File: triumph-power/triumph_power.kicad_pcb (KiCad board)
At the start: 2 copper layers, 43.2 x 30.5 mm, 13 parts, among them J1 JST_XH_vert_01x04, J2 JST_XH_vert_01x04

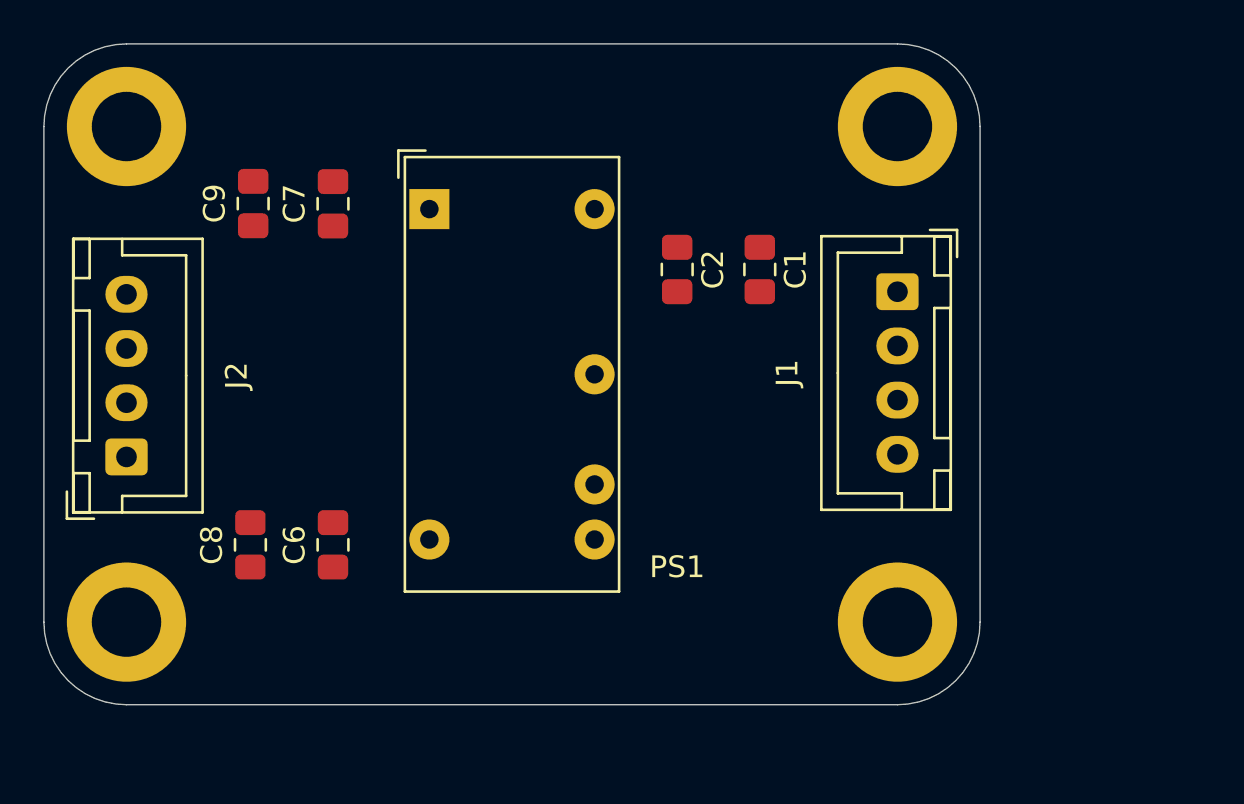
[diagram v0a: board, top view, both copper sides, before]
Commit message: Route power board
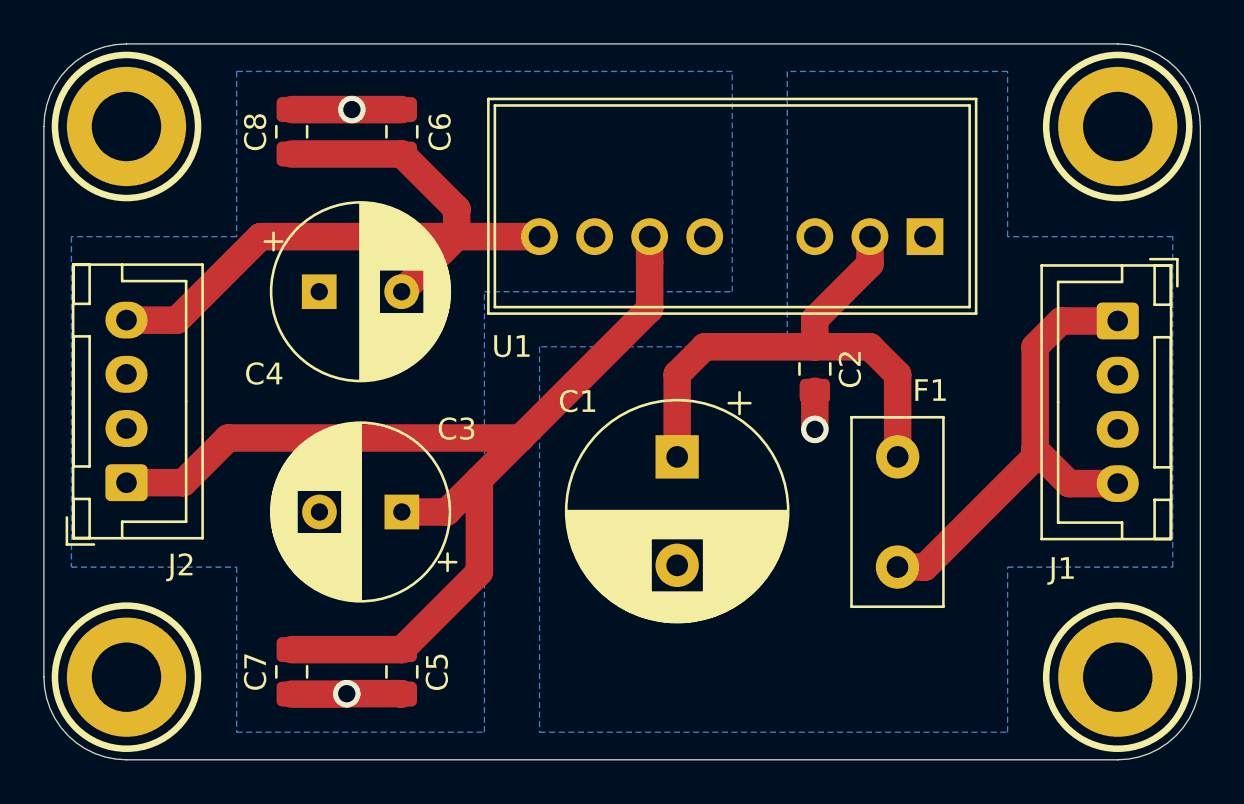
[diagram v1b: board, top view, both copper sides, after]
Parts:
- removed C9: 0.01uF, Capacitor_SMD:C_0805_2012Metric_Pad1.15x1.40mm_HandSolder
- removed PS1: RS-1212D, Converter_DCDC:Converter_DCDC_XP_POWER-IAxxxxD_THT
- added C3: 10uF, Capacitor_THT:CP_Radial_D8.0mm_P3.80mm, F.Cu at (139.7, 114.3)
- added C4: 10uF, Capacitor_THT:CP_Radial_D8.0mm_P3.80mm, F.Cu at (135.9, 104.1)
- added C5: 0.1uF, Capacitor_SMD:C_0805_2012Metric_Pad1.15x1.40mm_HandSolder, F.Cu at (139.7, 121.7)
- added F1: MF-R050, Fuse:Fuse_Littelfuse_395Series, F.Cu at (162.6, 116.8)
- added U1: RS-1212D, triumph:RS-xxxxD, F.Cu at (163.8, 101.6)
- C1: value 1uF -> 47uF; footprint Capacitor_SMD:C_0805_2012Metric_Pad1.15x1.40mm_HandSolder -> Capacitor_THT:CP_Radial_D10.0mm_P5.00mm
- C7: value 0.1uF -> 0.01uF
- moved C7 21.7 mm to (134.6, 121.7)
- moved C6 19.3 mm to (139.7, 96.8)
- moved C8 19.1 mm to (134.6, 96.8)
- moved REF** 10.5 mm to (172.7, 121.9)
- moved J1 10.2 mm to (172.7, 105.5)
- moved REF** 10.2 mm to (172.7, 96.5)
- moved C1 9.45 mm to (152.4, 111.8)
- moved C2 7.84 mm to (158.8, 107.7)
- moved REF** 2.54 mm to (127.0, 121.9)
- moved J2 1.19 mm to (127.0, 113.0)
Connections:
- C6 pad 1: +12V -> GND
- C6 pad 2: GND -> -12V
- C7 pad 1: GND -> +12V
- C7 pad 2: -12V -> GND
- C8 pad 1: +12V -> GND
- C8 pad 2: GND -> -12V
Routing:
- net +12V: track 0.00 -> 52.1 mm
- net -12V: track 0.00 -> 34.2 mm
- net Net-(C1-Pad1): track 0.00 -> 25.0 mm
- net VCC: track 0.00 -> 22.3 mm
- net GND: track 0.00 -> 10.2 mm, vias 0 -> 2
- net GNDREF: track 0.00 -> 1.76 mm, vias 0 -> 1
- added copper zone on B.Cu, net GND
- added copper zone on B.Cu, net GNDREF
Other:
- board size 43.2 x 30.5 mm -> 53.3 x 33 mm
- net class Power added: clearance 0.2, trace_width 1.27, via_dia 1.27, via_drill 0.8

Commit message: Add a prodigious quantity of PCB graphics
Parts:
- added G***: LOGO, triumph-logos:rs, B.Cu at (157.0, 110.7)
- added G***: LOGO, triumph-logos:cit-ee, B.Cu at (153.7, 121.4)
- added G***: LOGO, triumph-logos:triumph-logo-inv-small, F.Cu at (151.9, 122.2)
- C2, C5, C6, C7, C8: footprint Capacitor_SMD:C_0805_2012Metric_Pad1.15x1.40mm_HandSolder -> triumph:0805_C_HandSoldering
- moved C2 1.56 mm to (158.8, 109.3)
- moved C1 1.14 mm to (151.4, 111.3)
- moved F1 0.51 mm to (163.1, 116.8)
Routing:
- net Net-(C1-Pad1): track 25.0 -> 23.5 mm
- net GNDREF: track 1.76 -> 2.54 mm
- net VCC: track 22.3 -> 21.8 mm
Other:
- board text added: "+12V"
- board text added: "-12V"
- board text added: "GND"
- board text added: "Power Board Ray Sun EE 90"
- board text added: "VIN"

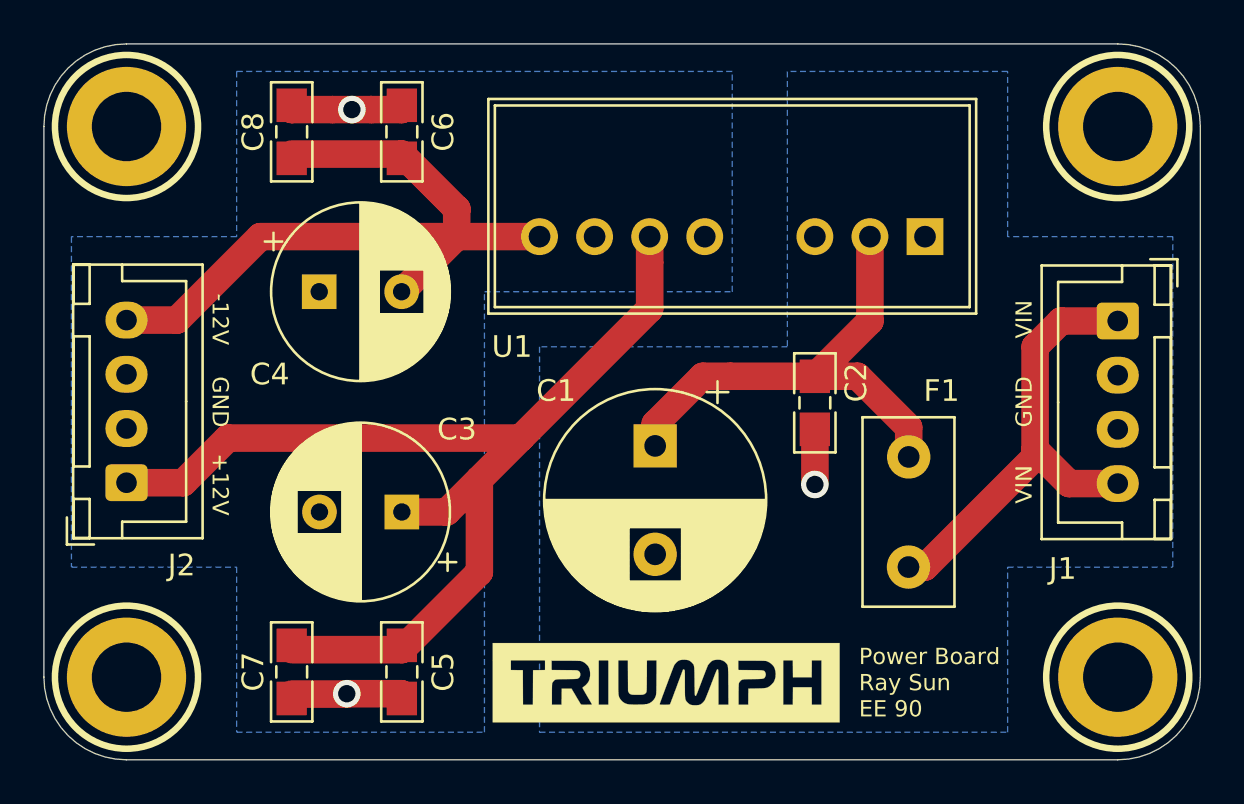
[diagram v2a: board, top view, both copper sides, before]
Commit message: Reroute power board
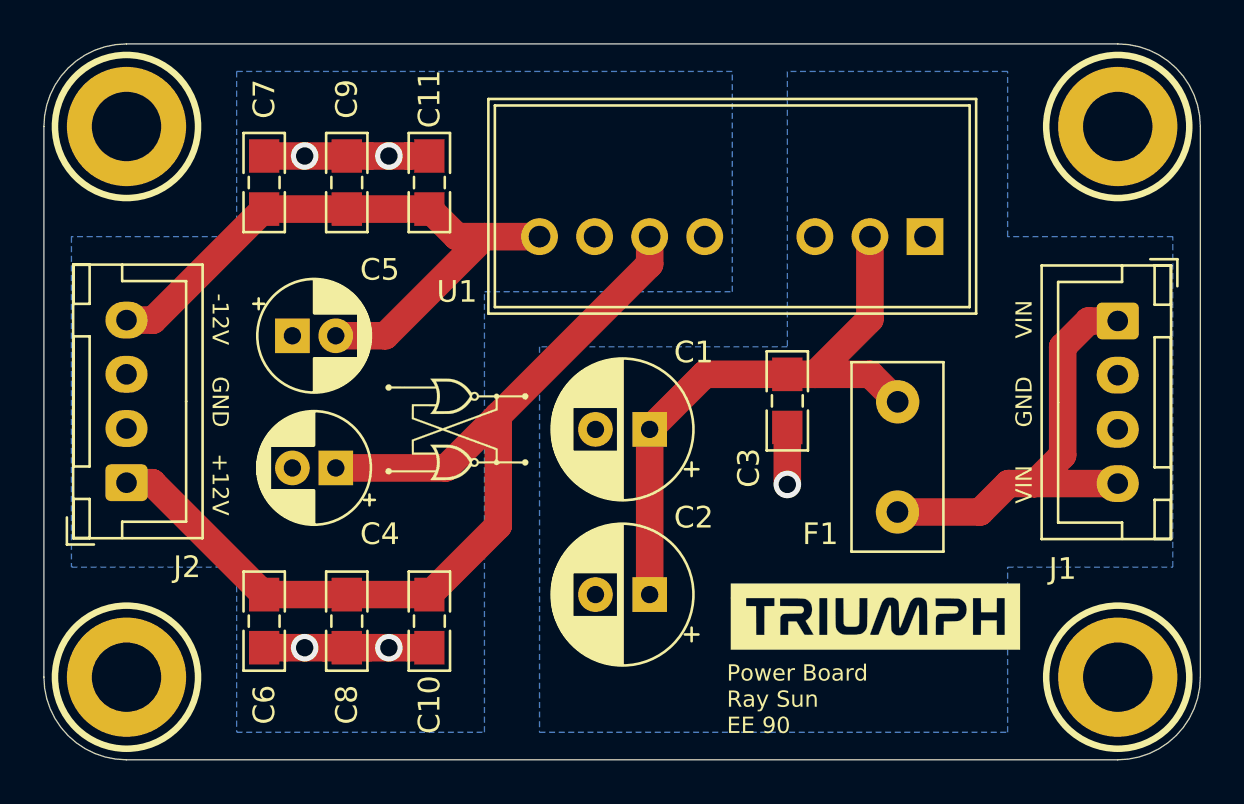
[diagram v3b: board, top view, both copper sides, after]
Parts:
- removed the G*** at (157.0, 110.7)
- removed the G*** at (151.9, 122.2)
- added C10: 0.01uF, triumph:0805_C_HandSoldering, F.Cu at (141.0, 119.3)
- added C11: 0.01uF, triumph:0805_C_HandSoldering, F.Cu at (141.0, 99.1)
- added C9: 0.1uF, triumph:0805_C_HandSoldering, F.Cu at (137.2, 99.1)
- added G***: LOGO, triumph-logos:rs-xs, F.Cu at (142.2, 110.5)
- added G***: LOGO, triumph-logos:triumph-logo-inv-xs, F.Cu at (161.5, 119.1)
- C1: footprint Capacitor_THT:CP_Radial_D10.0mm_P5.00mm -> Capacitor_THT:CP_Radial_D6.3mm_P2.50mm
- C2: value 0.1uF -> 47uF; footprint triumph:0805_C_HandSoldering -> Capacitor_THT:CP_Radial_D6.3mm_P2.50mm
- C3: value 10uF -> 0.1uF; footprint Capacitor_THT:CP_Radial_D8.0mm_P3.80mm -> triumph:0805_C_HandSoldering
- C4: footprint Capacitor_THT:CP_Radial_D8.0mm_P3.80mm -> Capacitor_THT:CP_Radial_D5.0mm_P2.00mm
- C5: value 0.1uF -> 10uF; footprint triumph:0805_C_HandSoldering -> Capacitor_THT:CP_Radial_D5.0mm_P2.00mm
- C6: value 0.1uF -> 1uF
- C7: value 0.01uF -> 1uF
- C8: value 0.01uF -> 0.1uF
- moved C6 23.4 mm to (133.3, 119.3)
- moved C8 22.7 mm to (137.2, 119.3)
- moved C7 22.6 mm to (133.3, 99.1)
- moved C3 18.5 mm to (157.5, 109.2), turned to 270 degrees
- moved C5 16.3 mm to (134.7, 106.2), turned to 0 degrees
- moved C2 11.7 mm to (151.1, 118.1), turned to 180 degrees
- moved C4 8.16 mm to (136.7, 112.3), turned to 180 degrees
- moved G*** 4.45 mm to (149.2, 121.5)
- moved F1 2.59 mm to (162.6, 114.3)
- moved C1 0.80 mm to (151.1, 110.5), turned to 180 degrees
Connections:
- C3 pad 1: +12V -> Net-(C1-Pad1)
- C3 pad 2: GND -> GNDREF
- C4 pad 1: GND -> +12V
- C4 pad 2: -12V -> GND
- C5 pad 1: +12V -> GND
- C5 pad 2: GND -> -12V
- C6 pad 1: GND -> +12V
- C6 pad 2: -12V -> GND
- C7 pad 1: +12V -> GND
- C7 pad 2: GND -> -12V
- C8 pad 1: GND -> +12V
- C8 pad 2: -12V -> GND
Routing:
- net +12V: track 52.1 -> 45.3 mm
- net GND: track 10.2 -> 15.2 mm, vias 2 -> 4
- net Net-(C1-Pad1): track 23.5 -> 28.0 mm
- net -12V: track 34.2 -> 30.4 mm
- net VCC: track 21.8 -> 20.6 mm

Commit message: Generate gerbers
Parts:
- moved C4 0.25 mm to (136.7, 112.5)
- moved C5 0.25 mm to (134.7, 105.9)
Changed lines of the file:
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@@
     (thickness 1.6)
     (drawings 23)
-    (tracks 61)
+    (tracks 63)
     (zones 0)
     (modules 22)
@@
     (solder_mask_min_width 0.25)
     (aux_axis_origin 0 0)
+    (grid_origin 123.19 125.73)
     (visible_elements 7FFFFFFF)
     (pcbplotparams
@@
   )
   (module Capacitor_THT:CP_Radial_D5.0mm_P2.00mm (layer F.Cu)
-    (at 134.652 106.172)
+    (at 134.652 105.918)
     (descr "CP, Radial series, Radial, pin pitch=2.00mm, , diameter=5mm, Electrolytic Capacitor")
     (tags "CP Radial series Radial pin pitch 2.00mm  diameter 5mm Electrolytic Capacitor")
@@
   )
   (module Capacitor_THT:CP_Radial_D5.0mm_P2.00mm (layer F.Cu)
-    (at 136.652 112.268 180)
+    (at 136.652 112.522 180)
     (descr "CP, Radial series, Radial, pin pitch=2.00mm, , diameter=5mm, Electrolytic Capacitor")
     (tags "CP Radial series Radial pin pitch 2.00mm  diameter 5mm Electrolytic Capacitor")
@@
   (segment (start 137.16 118.11) (end 140.97 118.11) (width 1.27) (layer F.Cu) (net 4))
   (segment (start 151.13 101.6) (end 151.13 102.87) (width 1.27) (layer F.Cu) (net 4))
-  (segment (start 141.732 112.268) (end 136.652 112.268) (width 1.27) (layer F.Cu) (net 4))
   (segment (start 144.145 109.855) (end 144.145 114.935) (width 1.27) (layer F.Cu) (net 4))
   (segment (start 151.13 102.87) (end 144.145 109.855) (width 1.27) (layer F.Cu) (net 4))
+  (segment (start 144.145 114.935) (end 140.97 118.11) (width 1.27) (layer F.Cu) (net 4))
+  (segment (start 136.906 112.268) (end 136.652 112.522) (width 1.27) (layer F.Cu) (net 4))
   (segment (start 144.145 109.855) (end 141.732 112.268) (width 1.27) (layer F.Cu) (net 4))
-  (segment (start 144.145 114.935) (end 140.97 118.11) (width 1.27) (layer F.Cu) (net 4))
-  (segment (start 138.938 106.172) (end 136.652 106.172) (width 1.27) (layer F.Cu) (net 5))
+  (segment (start 141.478 112.522) (end 141.732 112.268) (width 1.27) (layer F.Cu) (net 4))
+  (segment (start 136.652 112.522) (end 141.478 112.522) (width 1.27) (layer F.Cu) (net 4))
   (segment (start 146.05 101.6) (end 143.51 101.6) (width 1.27) (layer F.Cu) (net 5))
-  (segment (start 143.51 101.6) (end 138.938 106.172) (width 1.27) (layer F.Cu) (net 5))
   (segment (start 140.97 100.33) (end 142.24 101.6) (width 1.27) (layer F.Cu) (net 5))
   (segment (start 142.24 101.6) (end 143.51 101.6) (width 1.27) (layer F.Cu) (net 5))
@@
   (segment (start 128.23 105.45) (end 133.35 100.33) (width 1.27) (layer F.Cu) (net 5))
   (segment (start 127 105.45) (end 128.23 105.45) (width 1.27) (layer F.Cu) (net 5))
+  (segment (start 139.192 105.918) (end 136.652 105.918) (width 1.27) (layer F.Cu) (net 5))
+  (segment (start 143.51 101.6) (end 139.192 105.918) (width 1.27) (layer F.Cu) (net 5))
   (segment (start 166.37 114.3) (end 162.56 114.3) (width 1.27) (layer F.Cu) (net 6))
   (segment (start 167.68 112.99) (end 166.37 114.3) (width 1.27) (layer F.Cu) (net 6))
